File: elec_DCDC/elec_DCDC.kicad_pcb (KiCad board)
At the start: 2 copper layers, 20 x 20 mm, 17 parts, among them J1 JST SH, J7 JST SH, U1 AS5600L

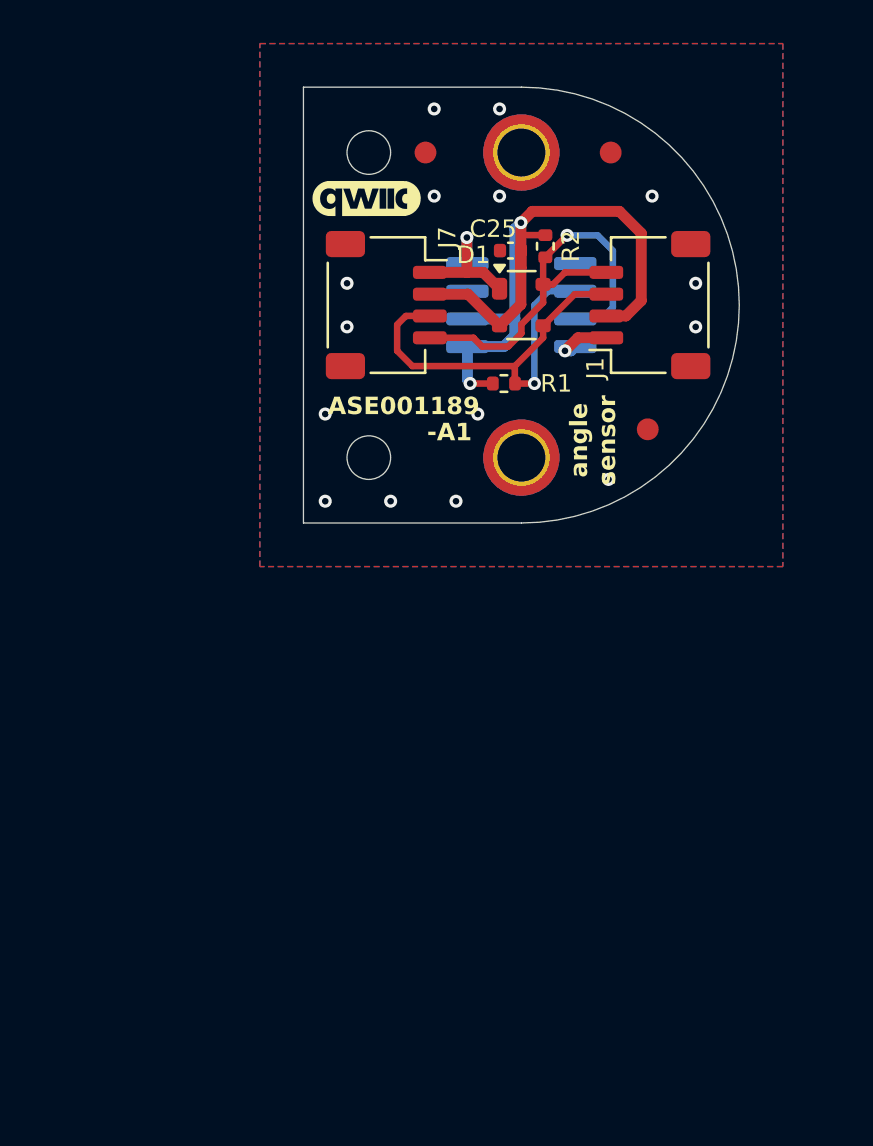
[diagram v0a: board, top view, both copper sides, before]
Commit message: [added] Gripette-specific DCDC
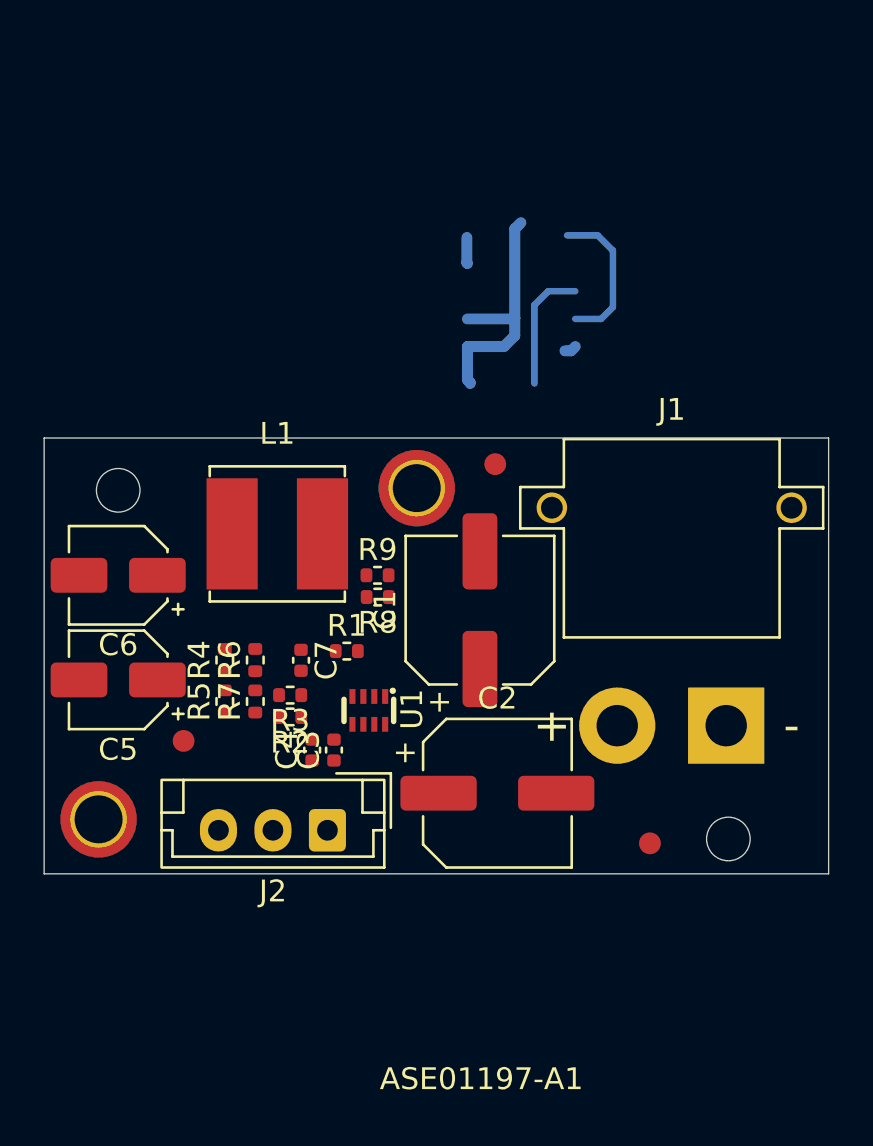
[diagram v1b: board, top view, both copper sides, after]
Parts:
- removed C25: 100n, Capacitor_SMD:C_0402_1005Metric
- removed D1: SP0503BAHT, Package_TO_SOT_SMD:SOT-143
- removed G1: qwiic_Logo, Library_Pollen:Logo_qwiic_5mm
- removed J7: JST SH, Connector_JST:JST_SH_SM04B-SRSS-TB_1x04-1MP_P1.00mm_Horizontal
- added C1: 10u 35V, Library_Pollen:CP_Elec_6.3x7.7, F.Cu at (129.0, 63.6)
- added C2: 10u 35V, Library_Pollen:CP_Elec_6.3x7.7, F.Cu at (129.8, 72.0)
- added C3: 22n, Capacitor_SMD:C_0402_1005Metric, F.Cu at (122.3, 70.1)
- added C4: 100n, Capacitor_SMD:C_0402_1005Metric, F.Cu at (121.3, 70.1)
- added C5: 22u 16V, Capacitor_SMD:CP_Elec_4x5.4, F.Cu at (112.4, 66.8)
- added C6: 22u 16V, Capacitor_SMD:CP_Elec_4x5.4, F.Cu at (112.4, 62.0)
- added C7: 100p 50V, Capacitor_SMD:C_0402_1005Metric, F.Cu at (120.8, 65.9)
- added J2: Dynamixel-3, Connector_JST:JST_EH_B3B-EH-A_1x03_P2.50mm_Vertical, F.Cu at (122.0, 73.7)
- added L1: 6,8u 3A, Inductor_SMD:L_Bourns_SRN6045TA, F.Cu at (119.7, 60.1)
- added R3: 0R, Resistor_SMD:R_0402_1005Metric, F.Cu at (120.3, 67.5)
- added R4: 120k, Resistor_SMD:R_0402_1005Metric, F.Cu at (117.3, 65.9)
- added R5: 9k1, Resistor_SMD:R_0402_1005Metric, F.Cu at (117.3, 67.8)
- added R6: 160k, Resistor_SMD:R_0402_1005Metric, F.Cu at (118.7, 65.9)
- added R7: 6k8, Resistor_SMD:R_0402_1005Metric, F.Cu at (118.7, 67.8)
- added R8: 100k, Resistor_SMD:R_0402_1005Metric, F.Cu at (124.3, 63.0)
- added R9: 51k, Resistor_SMD:R_0402_1005Metric, F.Cu at (124.3, 62.0)
- J1: value JST SH -> XT30; footprint Connector_JST:JST_SH_SM04B-SRSS-TB_1x04-1MP_P1.00mm_Horizontal -> Library_Pollen:AMASS_XT30PW-M_1x02_P2.50mm_Horizontal
- R1: value DNP-10k -> 10k
- R2: value DNP-10k -> DNP-0R
- U1: value AS5600L -> MP2338; footprint Package_SO:SOIC-8_3.9x4.9mm_P1.27mm -> LCSC_parts_lib:SOT-583-8_L2.1-W1.2-P0.50-LS1.6-BR; moved to F.Cu
- moved FID2 33.3 mm to (136.8, 74.3), turned to 90 degrees
- moved FID3 25.7 mm to (115.4, 69.6), turned to 90 degrees
- moved H5 25.5 mm to (111.5, 73.2), turned to 90 degrees
- moved R2 24.6 mm to (120.3, 68.5), turned to 180 degrees
- moved H6 24.1 mm to (140.4, 74.1)
- moved U1 19.9 mm to (123.9, 68.2), turned to 90 degrees
- moved J1 19.6 mm to (140.3, 68.9), turned to 0 degrees
- moved H7 19.3 mm to (112.4, 58.1), turned to 90 degrees
- moved H2 16.6 mm to (152.6, 43.8)
- moved H3 16.4 mm to (138.8, 44.2)
- moved H4 16.1 mm to (126.1, 58.0)
- moved FID1 15.3 mm to (129.7, 56.9), turned to 90 degrees
- moved R1 14.2 mm to (122.9, 65.5)
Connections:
- J1 pad 2: +3V3 -> Net-(J1-Pin_2)
- R1 pad 1: +3V3 -> Net-(U1-FB)
- R1 pad 2: Net-(J1-Pin_3) -> Net-(C7-Pad2)
- R2 pad 1: +3V3 -> Net-(C7-Pad2)
- R2 pad 2: Net-(J1-Pin_4) -> Net-(R2-Pad2)
- U1 pad 1: +3V3 -> Net-(U1-PG)
- U1 pad 2: +3V3 -> Net-(J1-Pin_2)
- U1 pad 3: unconnected-(U1-Out-Pad3) -> Net-(U1-SW)
- U1 pad 5: unconnected-(U1-PGO-Pad5) -> Net-(U1-BST)
- U1 pad 6: Net-(J1-Pin_3) -> Net-(J1-Pin_2)
- U1 pad 7: Net-(J1-Pin_4) -> Net-(U1-SS)
- U1 pad 8: GND -> Net-(U1-FB)
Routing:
- net +3V3: track 35.2 -> 0.00 mm, vias 2 -> 0
- net (no net): track 0.00 -> 24.3 mm
- net Net-(J1-Pin_3): track 21.9 -> 0.00 mm, vias 1 -> 0
- net Net-(J1-Pin_4): track 20.0 -> 0.00 mm, vias 1 -> 0
- net GND: track 9.02 -> 1.76 mm, vias 17 -> 0
- removed copper zone on B.Cu, net GND
- removed copper zone on F.Cu, net GND
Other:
- board size 20 x 20 mm -> 36 x 20 mm
- board text added: "ASE01197-A1"
- board text removed: "!! Prévoir une place pour marquer l'adresse I2C du capteur d'angle"
- board text removed: "-A1"
- board text removed: "ASE001189"
- board text removed: "angle sensor"
